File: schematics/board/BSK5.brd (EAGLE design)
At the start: 94 x 94 mm, 88 parts, among them U1 STM32F405RGT6, X1 JST-6, X11 JST-6

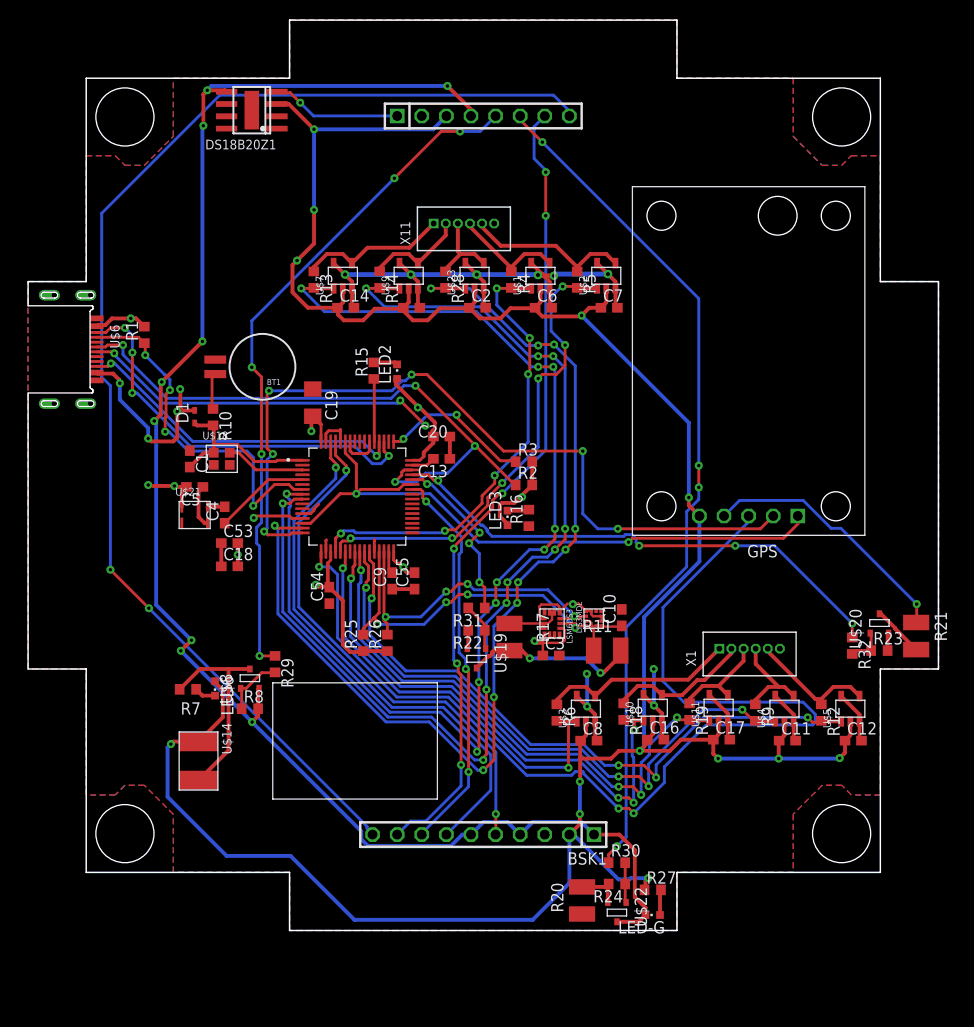
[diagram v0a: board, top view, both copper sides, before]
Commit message: Две линии i2c на платах БСК заменены на одну
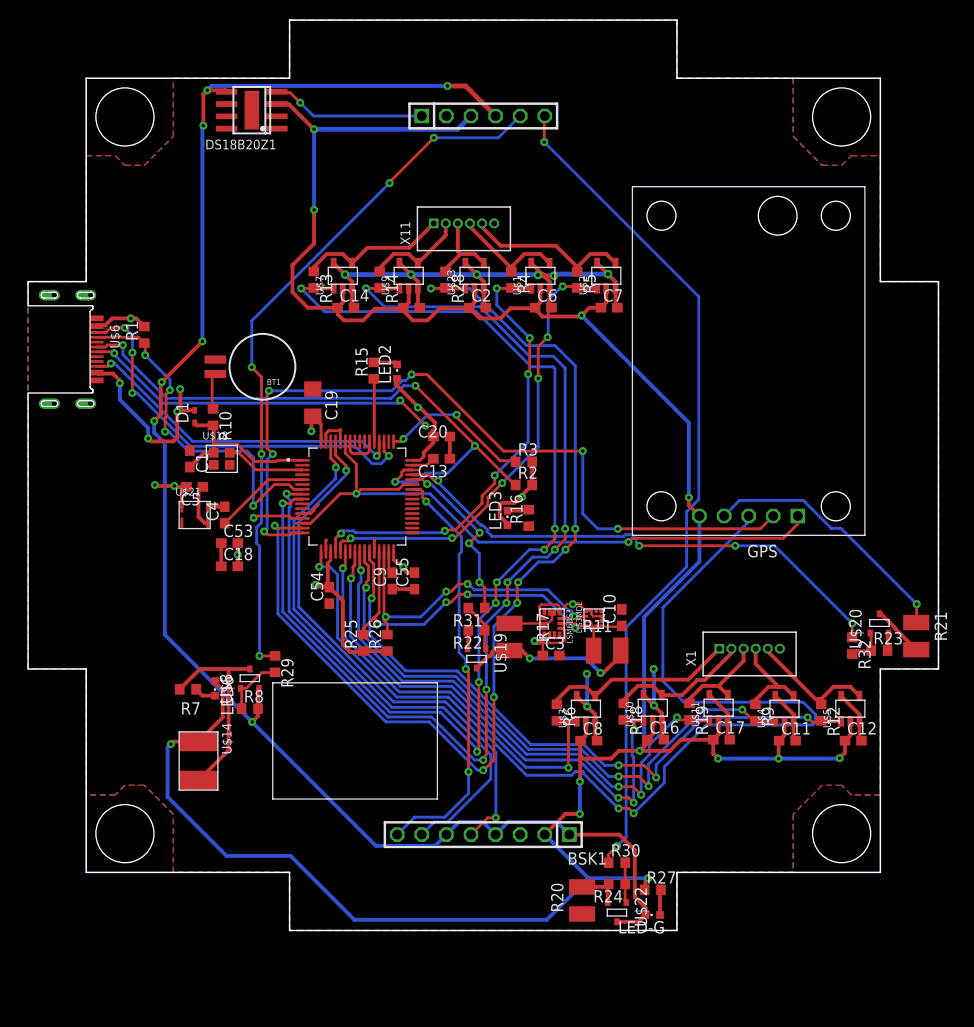
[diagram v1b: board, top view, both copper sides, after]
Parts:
- BSK1: device pinheadCS:1X10 -> pinheadCS:1X08
- BSK3: device pinheadCS:1X08 -> pinheadCS:1X06
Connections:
- removed net SCL-INA: BSK1.9, BSK3.7
- removed net SDA-INA: BSK1.10, BSK3.8
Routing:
- net SDA-INA: track 130.3 -> 0.00 mm, vias 2 -> 0
- net SCL-INA: track 83.2 -> 0.00 mm, vias 6 -> 0
- net 5V: track 275.5 -> 279.6 mm, vias 13 -> 12
- net TIME-ES: track 40.8 -> 43.6 mm
- net B5-KHEAT: track 70.9 -> 73.5 mm
- net 1W: track 13.5 -> 16.0 mm
- net SS3: track 49.2 -> 47.2 mm
- net SDA-TM: track 56.2 -> 58.0 mm
- net SCL-TM: track 54.6 -> 56.2 mm
- net SINS-KVCC: track 88.6 -> 87.6 mm, vias 4 -> 2
- net GND-OUT: track 166.5 -> 167.3 mm, vias 9 -> 7
- net 3V3: track 103.4 -> 102.7 mm
- net SS1: track 108.7 -> 108.5 mm, vias 10 -> 8
- net SS7: vias 10 -> 8
- net SS8: vias 10 -> 8

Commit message: Добавлена схема дозиметра, исправлены платы СБ
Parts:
- moved R1 2.01 mm to (12.2, 63.5)
- moved U$6 2.00 mm to (0.00, 62.0)
- moved C15 1.80 mm to (37.8, 64.4)
- moved C6 1.80 mm to (51.4, 64.4)
- moved R28 1.80 mm to (41.3, 67.3)
- moved R13 1.80 mm to (27.7, 67.3)
- moved C2 1.80 mm to (44.6, 64.4)
- moved C7 1.80 mm to (58.2, 64.2)
- moved R14 1.80 mm to (34.5, 67.3)
- moved C14 1.80 mm to (31.0, 64.3)
- moved R4 1.60 mm to (48.3, 67.3)
- moved R5 1.50 mm to (55.2, 67.3)
- moved U$23 1.24 mm to (44.9, 67.9), turned to 270 degrees
- moved U$9 1.24 mm to (38.1, 67.9), turned to 270 degrees
- moved U$10 1.20 mm to (65.7, 23.0), turned to 270 degrees
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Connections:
- net 5V: now also U$1.P$5, U$10.P$5, U$11.P$5, U$2.P$5, U$23.P$5, U$3.P$5, U$4.P$5, U$5.P$5, U$7.P$5, U$9.P$5; no longer U$1.P$2, U$10.P$2, U$11.P$2, U$2.P$2, U$23.P$2, U$3.P$2, U$4.P$2, U$5.P$2, U$7.P$2, U$9.P$2
- net GND: now also U$1.P$2, U$10.P$2, U$11.P$2, U$2.P$2, U$23.P$2, U$3.P$2, U$4.P$2, U$5.P$2, U$7.P$2, U$9.P$2; no longer U$1.P$5, U$10.P$5, U$11.P$5, U$2.P$5, U$23.P$5, U$3.P$5, U$4.P$5, U$5.P$5, U$7.P$5, U$9.P$5
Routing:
- net 5V: track 279.6 -> 299.3 mm
- net SS3: track 47.2 -> 57.1 mm
- net N$4: track 15.5 -> 24.3 mm
- net N$46: track 10.6 -> 18.7 mm
- net SS10: track 57.9 -> 65.3 mm
- net SS4: track 44.6 -> 51.6 mm, vias 2 -> 4
- net SS9: track 56.0 -> 62.9 mm
- net N$47: track 14.7 -> 21.6 mm
- net SS5: track 63.2 -> 69.4 mm
- net SS7: track 116.6 -> 122.2 mm
- net N$5: track 20.2 -> 25.7 mm
- net SS2: track 47.4 -> 52.6 mm
- net N$48: track 10.3 -> 15.4 mm
- net N$45: track 8.50 -> 13.3 mm
- net SS8: track 112.8 -> 117.0 mm
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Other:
- outline, holes or cut-outs redrawn

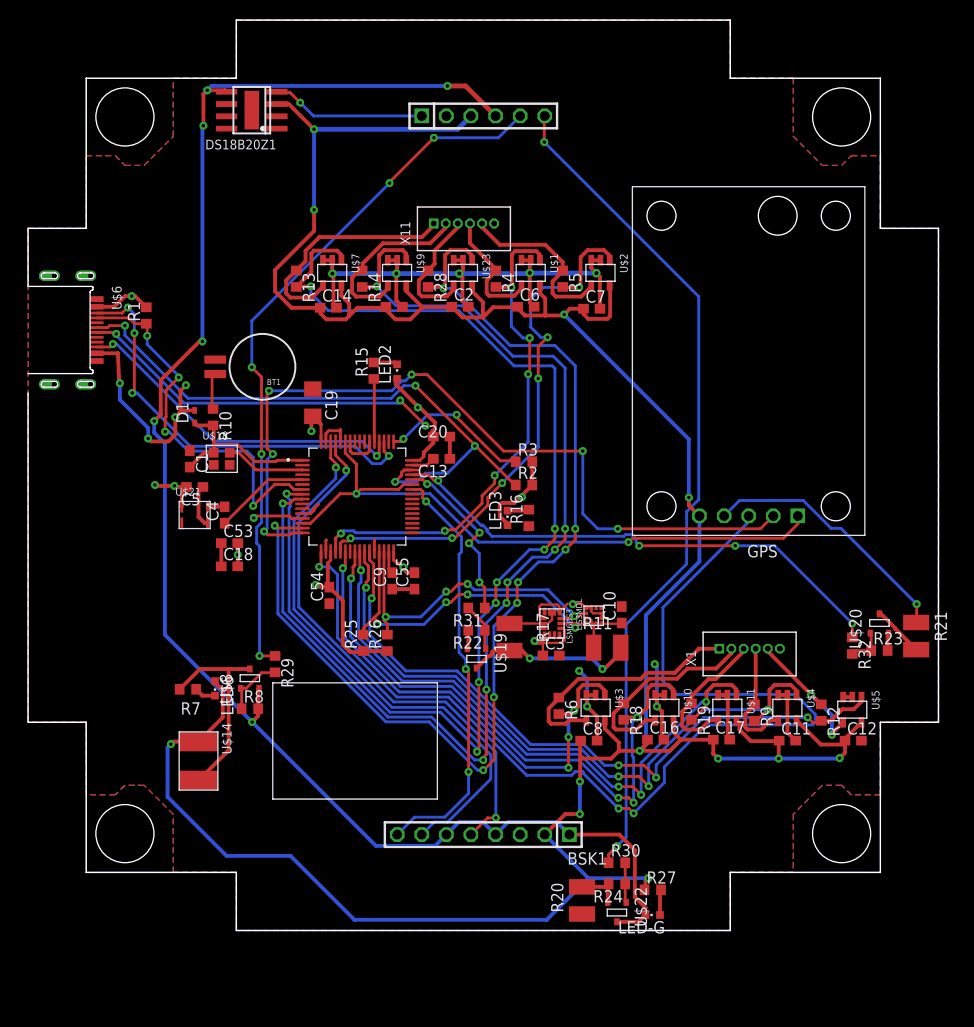
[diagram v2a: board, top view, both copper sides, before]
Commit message: Обновлен список плат, работа над платой ПН
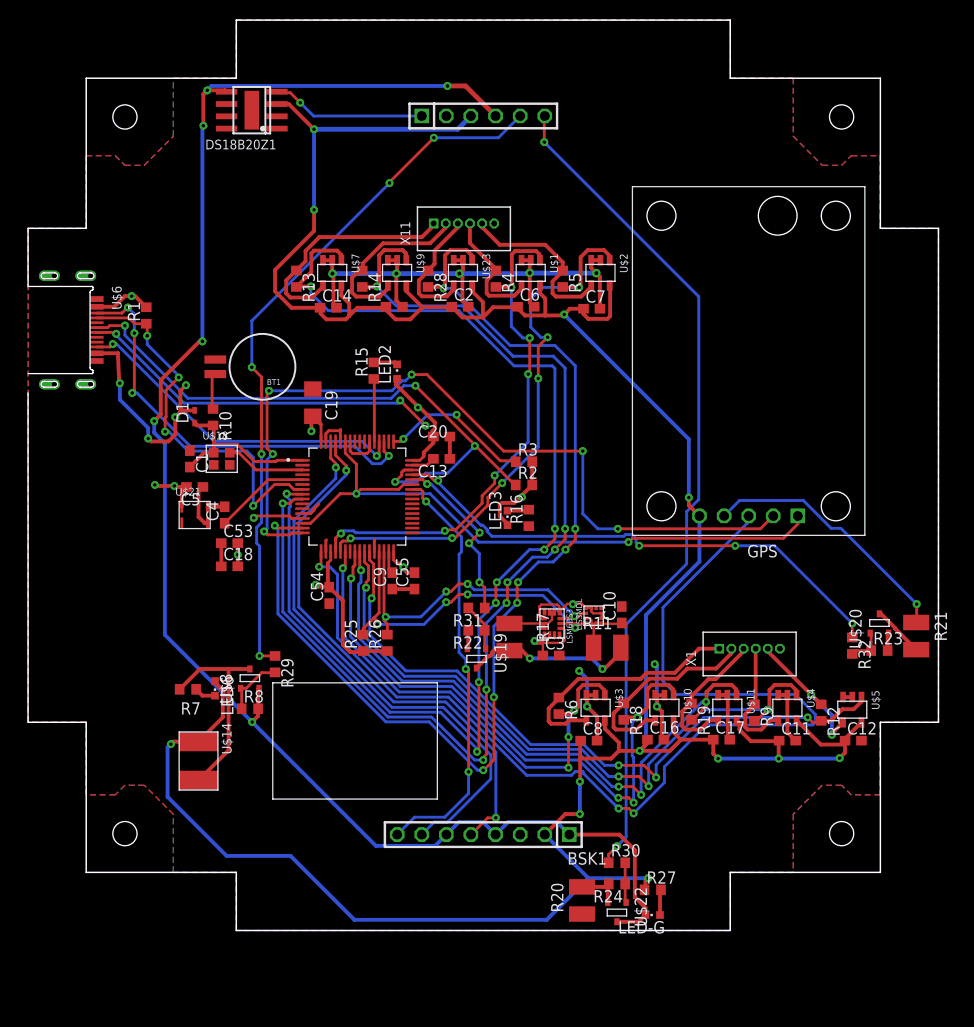
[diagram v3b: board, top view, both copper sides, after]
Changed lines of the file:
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@@
 <wire x1="6" y1="6" x2="21.5" y2="6" width="0.1524" layer="20"/>
 <wire x1="21.5" y1="6" x2="21.5" y2="0" width="0.1524" layer="20"/>
-<hole x="10" y="10" drill="6"/>
-<hole x="84" y="84" drill="6"/>
-<hole x="10" y="84" drill="6"/>
-<hole x="84" y="10" drill="6"/>
+<hole x="10" y="10" drill="2.5"/>
+<hole x="84" y="84" drill="2.5"/>
+<hole x="10" y="84" drill="2.5"/>
+<hole x="84" y="10" drill="2.5"/>
 <wire x1="25.262" y1="25.572" x2="42.262" y2="25.572" width="0.1" layer="21"/>
 <wire x1="42.262" y1="25.572" x2="42.262" y2="13.572" width="0.1" layer="21"/>

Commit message: Схема БКУ
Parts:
- removed U$6: USB-C, CanCubeSat:USB-C
- added U$12: FFC-CONNECT68611, CanCubeSat:68611
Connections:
- net 3V3: now also U$12.P$1, U$12.P$2; no longer U$6.3V3/BUS0, U$6.3V3/BUS1
- net GND: no longer U$6.GND0, U$6.GND1
- net GND-OUT: now also U$12.P$10, U$12.P$4, U$12.P$6, U$12.P$8
- net NRST: now also U$12.P$3; no longer U$6.NRST/EN
- net RX-S: now also U$12.P$5; no longer U$6.RX0
- net SWC: now also U$12.P$11; no longer U$6.SWC/TXD
- net SWD: now also U$12.P$9; no longer U$6.SWD/RXD
- net TX-S: now also U$12.P$7; no longer U$6.TX0
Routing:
- net 3V3: track 106.1 -> 102.1 mm
- net NRST: track 39.9 -> 36.6 mm
- net RX-S: track 44.2 -> 41.6 mm
- net SWC: track 54.9 -> 52.9 mm
- net TX-S: track 35.4 -> 34.0 mm
- net SWD: track 64.1 -> 63.0 mm

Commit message: Исправлена БСК5
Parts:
- moved U$12 63.5 mm to (4.40, 61.0), flipped to the bottom, turned to 90 degrees
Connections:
- net GND-OUT: now also U$12.P$3, U$12.P$5, U$12.P$7, U$12.P$9; no longer U$12.P$10, U$12.P$4, U$12.P$6, U$12.P$8
- net NRST: now also U$12.P$11; no longer U$12.P$3
- net RX-S: now also U$12.P$4; no longer U$12.P$5
- net SWC: now also U$12.P$10; no longer U$12.P$11
- net SWD: now also U$12.P$8; no longer U$12.P$9
- net TX-S: now also U$12.P$6; no longer U$12.P$7
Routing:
- net GND-OUT: track 167.4 -> 192.5 mm, vias 6 -> 8
- net SWC: track 52.9 -> 63.9 mm
- net NRST: track 36.6 -> 44.9 mm, vias 4 -> 5
- net TX-S: track 34.0 -> 40.6 mm, vias 2 -> 3
- net SWD: track 63.0 -> 68.3 mm, vias 4 -> 5
- net RX-S: track 41.6 -> 41.5 mm, vias 4 -> 3

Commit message: На платах БСК устройства по умолчанию подтянуты к питанию
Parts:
- removed R23: 1M, resistor:R0603
- added R33: 1M, resistor:R0603
- moved R22 41.9 mm to (88.1, 28.6)
- moved R24 29.9 mm to (46.3, 31.0), turned to 0 degrees
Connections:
- net 11: no longer R24.2
- net 3V3: now also R22.1, R24.1, R33.1
- net GND: no longer R22.2, R23.2
- net N$10: now also R33.2; no longer R24.1
- net N$11: now also R24.2; no longer R22.1
- net N$13: now also R22.2; no longer R23.1
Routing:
- net 3V3: track 102.1 -> 124.6 mm, vias 16 -> 21
- net GND: track 116.4 -> 112.9 mm
- net 11: track 4.82 -> 3.31 mm
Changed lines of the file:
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@@
 <attribute name="NAME" x="48.1288" y="30.7162" size="1.27" layer="25" ratio="10" rot="R270"/>
-</element>
-<element name="R22" library="resistor" package="R0603" package3d_urn="urn:adsk.eagle:package:23555/3" value="1M" x="46.3" y="31" smashed="yes" rot="R180">
-<attribute name="NAME" x="46.935" y="30.365" size="1.27" layer="25" rot="R180"/>
-<attribute name="VALUE" x="46.935" y="32.905" size="1.27" layer="27" rot="R180"/>
 </element>
 <element name="U$20" library="CanCubeSat" package="SOT23-3" value="SI2302CDS" x="87.9" y="31.7" smashed="yes">
 <attribute name="NAME" x="86.0712" y="29.0838" size="1.27" layer="25" ratio="10" rot="R90"/>
-</element>
-<element name="R23" library="resistor" package="R0603" package3d_urn="urn:adsk.eagle:package:23555/3" value="1M" x="87.9" y="28.9" smashed="yes">
-<attribute name="NAME" x="87.265" y="29.535" size="1.27" layer="25"/>
-<attribute name="VALUE" x="87.265" y="26.995" size="1.27" layer="27"/>
 </element>
 <element name="U$21" library="CanCubeSat" package="Q24" value="Q24" x="17.2" y="42.9" smashed="yes">
@@
 <attribute name="NAME" x="62.6288" y="4.5162" size="1.27" layer="25" ratio="10" rot="R270"/>
 </element>
-<element name="R24" library="resistor" package="R0603" package3d_urn="urn:adsk.eagle:package:23555/3" value="1M" x="60.8" y="4.8" smashed="yes" rot="R180">
-<attribute name="NAME" x="61.435" y="4.165" size="1.27" layer="25" rot="R180"/>
-<attribute name="VALUE" x="61.435" y="6.705" size="1.27" layer="27" rot="R180"/>
-</element>
 <element name="R27" library="resistor" package="R0603" package3d_urn="urn:adsk.eagle:package:23555/3" value="2k" x="64.5" y="4.2" smashed="yes">
 <attribute name="NAME" x="63.865" y="4.835" size="1.27" layer="25"/>
@@
 </element>
 <element name="U$12" library="CanCubeSat" package="68611" value="FFC-CONNECT68611" x="4.4" y="61" smashed="yes" rot="MR90"/>
+<element name="R33" library="resistor" package="R0603" package3d_urn="urn:adsk.eagle:package:23555/3" value="1M" x="60.8" y="4.7" smashed="yes">
+<attribute name="NAME" x="60.165" y="5.335" size="1.27" layer="25"/>
+<attribute name="VALUE" x="60.165" y="2.795" size="1.27" layer="27"/>
+</element>
+<element name="R24" library="resistor" package="R0603" package3d_urn="urn:adsk.eagle:package:23555/3" value="1M" x="46.3" y="31" smashed="yes">
+<attribute name="NAME" x="45.665" y="31.635" size="1.27" layer="25"/>
+<attribute name="VALUE" x="45.665" y="29.095" size="1.27" layer="27"/>
+</element>
+<element name="R22" library="resistor" package="R0603" package3d_urn="urn:adsk.eagle:package:23555/3" value="1M" x="88.1" y="28.6" smashed="yes" rot="R180">
+<attribute name="NAME" x="88.735" y="27.965" size="1.27" layer="25" rot="R180"/>
+<attribute name="VALUE" x="88.735" y="30.505" size="1.27" layer="27" rot="R180"/>
+</element>
 </elements>
 <signals>
@@
 <contactref element="C3" pad="2"/>
 <contactref element="U$19" pad="2"/>
-<contactref element="R22" pad="2"/>
 <contactref element="U$20" pad="2"/>
-<contactref element="R23" pad="2"/>
 <contactref element="C5" pad="1"/>
 <contactref element="U$21" pad="P$2"/>
@@
 <contactref element="X1" pad="6"/>
 <wire x1="88.85" y1="30.7" x2="88.75" y2="30.6" width="0.4" layer="1"/>
-<wire x1="88.75" y1="30.6" x2="88.75" y2="28.9" width="0.4" layer="1"/>
 <wire x1="86.05" y1="19.6" x2="85.85" y2="19.8" width="0.4" layer="1"/>
 <wire x1="72.25" y1="19.9" x2="72.45" y2="19.7" width="0.4" layer="1"/>
@@
 <wire x1="37.6" y1="35.25" x2="39.9" y2="35.25" width="0.4" layer="1"/>
 <wire x1="43.55" y1="51" x2="43.55" y2="48.7" width="0.4" layer="1"/>
-<wire x1="45.45" y1="31" x2="45.45" y2="29.2" width="0.4" layer="1"/>
 <wire x1="45.45" y1="29.2" x2="45.35" y2="29.1" width="0.4" layer="1"/>
 <wire x1="30.75" y1="40.25" x2="30.75" y2="39.13" width="0.3" layer="1"/>
@@
 <wire x1="44.25" y1="53.25" x2="44.25" y2="53" width="0.3" layer="1"/>
 <wire x1="41.25" y1="53.25" x2="44.25" y2="53.25" width="0.3" layer="16"/>
-<wire x1="38.75" y1="50.75" x2="40.6" y2="52.6" width="0.3" layer="16"/>
-<wire x1="40.6" y1="52.6" x2="41.25" y2="53.25" width="0.3" layer="16"/>
+<wire x1="38.75" y1="50.75" x2="41.25" y2="53.25" width="0.3" layer="16"/>
 <wire x1="38.5" y1="50.5" x2="38.75" y2="50.75" width="0.3" layer="1"/>
 <wire x1="37.75" y1="50.5" x2="38.5" y2="50.5" width="0.3" layer="1"/>
@@
 <wire x1="10" y1="62.1" x2="10" y2="61.35398125" width="0.3" layer="16"/>
 <wire x1="16.426990625" y1="54.926990625" x2="10" y2="61.35398125" width="0.3" layer="16"/>
-<wire x1="40.6" y1="52.55398125" x2="40.6" y2="52.6" width="0.3" layer="16"/>
 <contactref element="U$12" pad="P$10"/>
 <wire x1="44.25" y1="53.25" x2="40.7" y2="56.8" width="0.3" layer="1"/>
@@
 <signal name="11">
 <contactref element="U$22" pad="2"/>
-<contactref element="R24" pad="2"/>
 <contactref element="R20" pad="2"/>
-<wire x1="59.85" y1="2.9" x2="59.85" y2="4.7" width="0.4" layer="1"/>
-<wire x1="59.85" y1="4.7" x2="59.95" y2="4.8" width="0.4" layer="1"/>
-<wire x1="59.95" y1="4.8" x2="59.65" y2="4.5" width="0.4" layer="1"/>
-<wire x1="59.65" y1="4.5" x2="57.2" y2="4.5" width="0.4" layer="1"/>
+<wire x1="59.85" y1="2.9" x2="58.8" y2="2.9" width="0.3" layer="1"/>
+<wire x1="58.8" y1="2.9" x2="57.2" y2="4.5" width="0.3" layer="1"/>
 </signal>
 <signal name="3V3">
@@
 <wire x1="5.05" y1="55" x2="5.05" y2="54" width="0.5" layer="16"/>
 <wire x1="8.775" y1="55" x2="5.05" y2="55" width="0.5" layer="16"/>
+<contactref element="R33" pad="1"/>
+<contactref element="R24" pad="1"/>
+<contactref element="R22" pad="1"/>
+<wire x1="88.95" y1="28.6" x2="88.95" y2="27.25" width="0.4" layer="1"/>
+<wire x1="88.95" y1="27.25" x2="88.9" y2="27.2" width="0.4" layer="1"/>
+<via x="88.9" y="27.2" extent="1-16" drill="0.35"/>
+<wire x1="59.95" y1="4.7" x2="59.95" y2="5.25" width="0.4" layer="1"/>
+<wire x1="59.95" y1="5.25" x2="58.4" y2="6.8" width="0.4" layer="1"/>
+<via x="58.4" y="6.8" extent="1-16" drill="0.35"/>
+<wire x1="45.45" y1="31" x2="43.75" y2="32.7" width="0.4" layer="1"/>
+<wire x1="43.75" y1="32.7" x2="43.725" y2="32.7" width="0.4" layer="1"/>
+<via x="43.725" y="32.7" extent="1-16" drill="0.35"/>
+<wire x1="43.725" y1="32.7" x2="43.725" y2="27.95" width="0.4" layer="16"/>
+<wire x1="43.725" y1="27.95" x2="44.1" y2="27.575" width="0.4" layer="16"/>
+<via x="44.1" y="27.575" extent="1-16" drill="0.35"/>
+<wire x1="44.1" y1="27.575" x2="44.1" y2="17.5" width="0.4" layer="1"/>
+<wire x1="44.1" y1="17.5" x2="44.5" y2="17.1" width="0.4" layer="1"/>
+<via x="44.5" y="17.1" extent="1-16" drill="0.35"/>
 </signal>
 <signal name="SINS-KVCC">
@@
 <contactref element="R30" pad="2"/>
 <contactref element="U$22" pad="1"/>
-<contactref element="R24" pad="1"/>
-<wire x1="61.65" y1="7" x2="61.65" y2="4.8" width="0.3" layer="1"/>
-<wire x1="61.65" y1="4.8" x2="61.65" y2="3" width="0.3" layer="1"/>
-<wire x1="61.65" y1="3" x2="61.75" y2="2.9" width="0.3" layer="1"/>
+<contactref element="R33" pad="2"/>
+<wire x1="61.75" y1="2.9" x2="61.75" y2="4.6" width="0.3" layer="1"/>
+<wire x1="61.75" y1="4.6" x2="61.65" y2="4.7" width="0.3" layer="1"/>
+<wire x1="61.65" y1="4.7" x2="61.65" y2="7" width="0.3" layer="1"/>
 </signal>
 <signal name="N$11">
 <contactref element="R31" pad="2"/>
 <contactref element="U$19" pad="1"/>
-<contactref element="R22" pad="1"/>
-<wire x1="45.45" y1="33.3" x2="47.15" y2="31.6" width="0.3" layer="1"/>
-<wire x1="47.15" y1="31.6" x2="47.15" y2="31" width="0.3" layer="1"/>
-<wire x1="47.15" y1="31" x2="47.15" y2="29.2" width="0.3" layer="1"/>
-<wire x1="47.15" y1="29.2" x2="47.25" y2="29.1" width="0.3" layer="1"/>
+<contactref element="R24" pad="2"/>
+<wire x1="47.15" y1="31" x2="45.45" y2="32.7" width="0.3" layer="1"/>
+<wire x1="45.45" y1="32.7" x2="45.45" y2="33.3" width="0.3" layer="1"/>
+<wire x1="47.25" y1="29.1" x2="47.15" y2="29.2" width="0.3" layer="1"/>
+<wire x1="47.15" y1="29.2" x2="47.15" y2="31" width="0.3" layer="1"/>
 </signal>
 <signal name="N$13">
-<contactref element="R23" pad="1"/>
 <contactref element="U$20" pad="1"/>
 <contactref element="R32" pad="2"/>
-<wire x1="86.95" y1="30.7" x2="87.05" y2="30.6" width="0.3" layer="1"/>
-<wire x1="87.05" y1="30.6" x2="87.05" y2="28.9" width="0.3" layer="1"/>
-<wire x1="87.05" y1="28.9" x2="85.45" y2="28.9" width="0.3" layer="1"/>
-<wire x1="85.45" y1="28.9" x2="85.1" y2="28.55" width="0.3" layer="1"/>
+<contactref element="R22" pad="2"/>
+<wire x1="86.95" y1="30.7" x2="87.25" y2="30.4" width="0.3" layer="1"/>
+<wire x1="87.25" y1="30.4" x2="87.25" y2="28.6" width="0.3" layer="1"/>
+<wire x1="87.25" y1="28.6" x2="85.15" y2="28.6" width="0.3" layer="1"/>
+<wire x1="85.15" y1="28.6" x2="85.1" y2="28.55" width="0.3" layer="1"/>
 </signal>
 </signals>
